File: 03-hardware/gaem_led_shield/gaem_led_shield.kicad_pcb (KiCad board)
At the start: 2 copper layers, 15 parts, among them J2 Conn_01x02, J3 Conn_01x02, J4 Conn_01x08

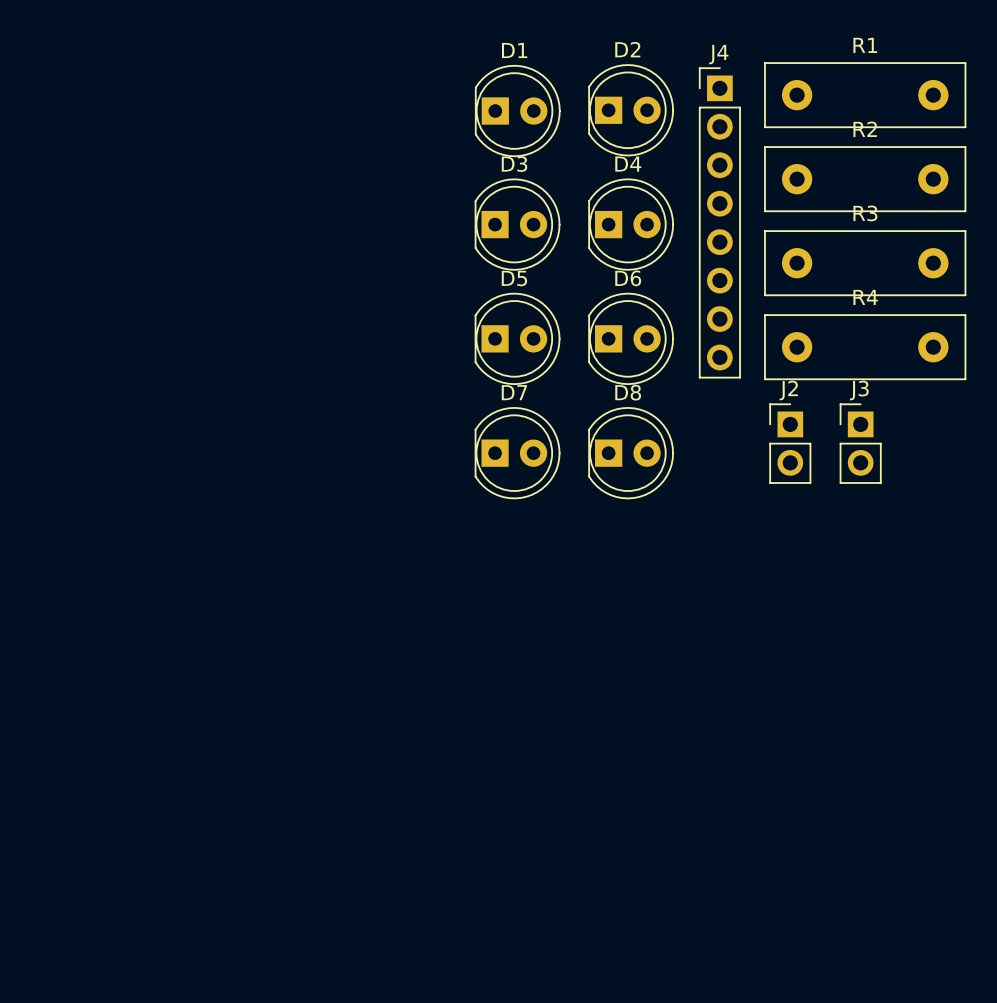
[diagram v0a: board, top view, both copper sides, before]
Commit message: Add LED shield v1.1 PCB layout
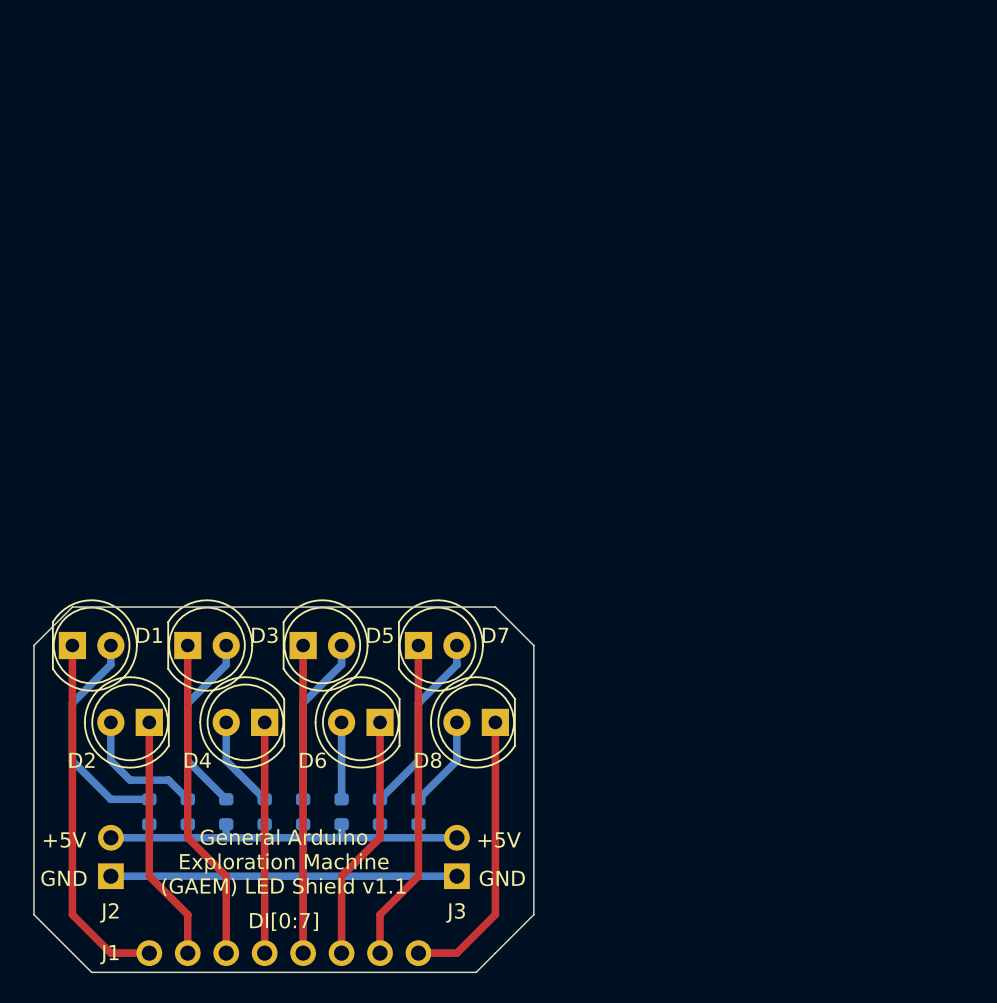
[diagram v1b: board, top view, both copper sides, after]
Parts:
- added R5: R, Resistor_SMD:R_0603_1608Metric, B.Cu at (119.4, 115.1)
- added R6: R, Resistor_SMD:R_0603_1608Metric, B.Cu at (121.9, 115.1)
- added R7: R, Resistor_SMD:R_0603_1608Metric, B.Cu at (124.5, 115.1)
- added R8: R, Resistor_SMD:R_0603_1608Metric, B.Cu at (127.0, 115.1)
- J1: renamed from J4; moved to B.Cu
- J2, J3: moved to B.Cu
- R1, R2, R3, R4: footprint Resistor_THT:R_Box_L13.0mm_W4.0mm_P9.00mm -> Resistor_SMD:R_0603_1608Metric; moved to B.Cu
- moved J1 68.4 mm to (109.2, 124.5), turned to -90 degrees
- moved R1 63.8 mm to (109.2, 115.1), turned to 90 degrees
- moved R2 58.0 mm to (111.8, 115.1), turned to 90 degrees
- moved J2 53.9 mm to (106.7, 119.4)
- moved R3 52.3 mm to (114.3, 115.1), turned to 90 degrees
- moved D2 50.6 mm to (109.2, 109.2), turned to 180 degrees
- moved R4 46.7 mm to (116.8, 115.1), turned to 90 degrees
- moved D1 45.0 mm to (104.1, 104.1)
- moved J3 40.0 mm to (129.5, 119.4)
- moved D4 40.0 mm to (116.8, 109.2), turned to 180 degrees
- moved D3 34.4 mm to (111.8, 104.1)
- moved D6 29.5 mm to (124.5, 109.2), turned to 180 degrees
- moved D5 23.9 mm to (119.4, 104.1)
- moved D8 19.3 mm to (132.1, 109.2), turned to 180 degrees
- moved D7 13.7 mm to (127.0, 104.1)
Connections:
- D2 pad 2: Net-(D1-A) -> Net-(D2-A)
- D4 pad 2: Net-(D3-A) -> Net-(D4-A)
- D6 pad 2: Net-(D5-A) -> Net-(D6-A)
- D8 pad 2: Net-(D7-A) -> Net-(D8-A)
- R2 pad 2: Net-(D3-A) -> Net-(D2-A)
- R3 pad 2: Net-(D5-A) -> Net-(D3-A)
- R4 pad 2: Net-(D7-A) -> Net-(D4-A)
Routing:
- net +5V: track 0.00 -> 30.0 mm
- net /DI1: track 0.00 -> 23.9 mm
- net GND: track 0.00 -> 22.9 mm
- net /DI7: track 0.00 -> 21.4 mm
- net /DI3: track 0.00 -> 21.4 mm
- net /DI5: track 0.00 -> 20.3 mm
- net /DI8: track 0.00 -> 18.8 mm
- net /DI2: track 0.00 -> 16.3 mm
- net /DI6: track 0.00 -> 16.3 mm
- net /DI4: track 0.00 -> 15.2 mm
- net Net-(D1-A): track 0.00 -> 14.8 mm
- net Net-(D7-A): track 0.00 -> 12.3 mm
- net Net-(D3-A): track 0.00 -> 12.3 mm
- net Net-(D5-A): track 0.00 -> 11.2 mm
- net Net-(D2-A): track 0.00 -> 8.67 mm
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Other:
- board outline added: 33 x 24.1 mm
- board text added: "+5V"
- board text added: "DI[0:7]"
- board text added: "GND"
- board text added: "General Arduino Exploration Machine (GAEM) LED Shield v1.1"
